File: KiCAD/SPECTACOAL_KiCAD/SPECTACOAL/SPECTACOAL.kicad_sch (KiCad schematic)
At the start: 22 parts, among them SW1 Reset, SW2 Reset, U1 TiVa, U2 Joystick_2_Axis_1SW, U3 Joystick_2_Axis_1SW, U4 D168K

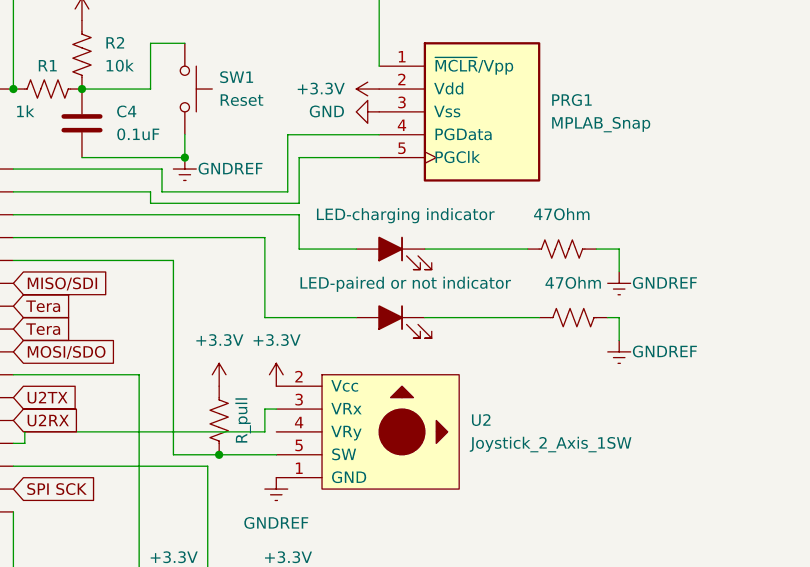
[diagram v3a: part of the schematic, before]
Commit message: change LED definitions
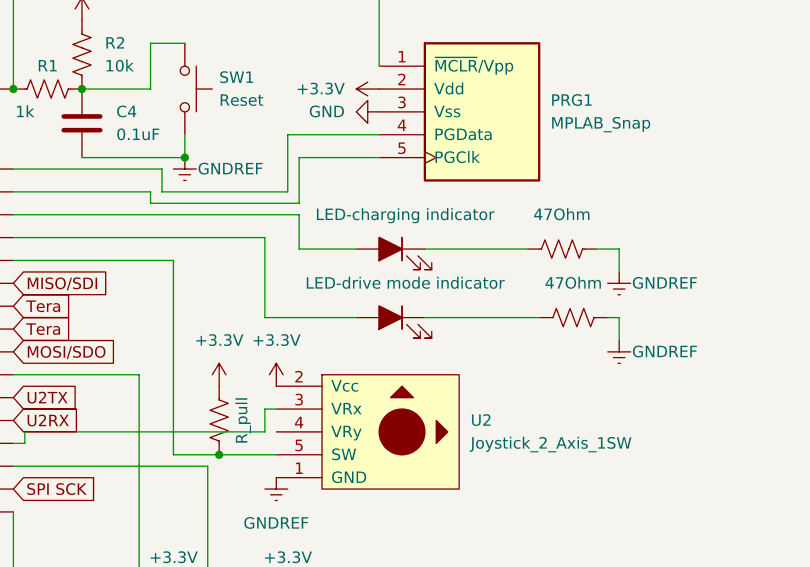
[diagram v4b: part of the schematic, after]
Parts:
- D2: value LED-paired or not indicator -> LED-drive mode indicator
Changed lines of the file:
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@@
       (effects (font (size 1.27 1.27)) hide)
     )
-    (property "Value" "LED-paired or not indicator" (at 193.3702 80.01 0)
+    (property "Value" "LED-drive mode indicator" (at 193.3702 80.01 0)
       (effects (font (size 1.27 1.27)))
     )
